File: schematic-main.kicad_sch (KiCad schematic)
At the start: 14 parts, among them J1 Fell_Cell_Conn_01x02_Pin, J2 CAN, J3 P_Valve, J4 Fan_2, J5 PWM_Out, J6 Fan_1, J7 Axilary_Out, J8 Temp, J9 Analog_In, P1 USB_C_Plug_USB2.0

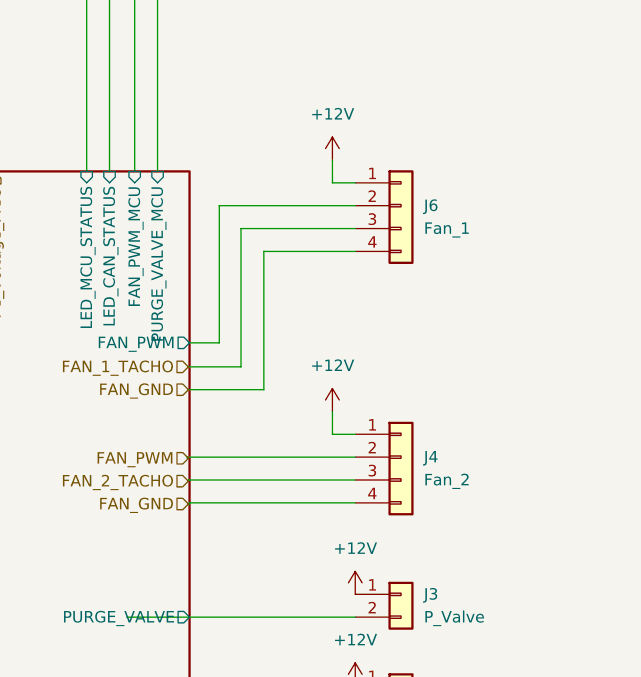
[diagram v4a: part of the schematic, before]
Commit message: First pcb, change fan conector
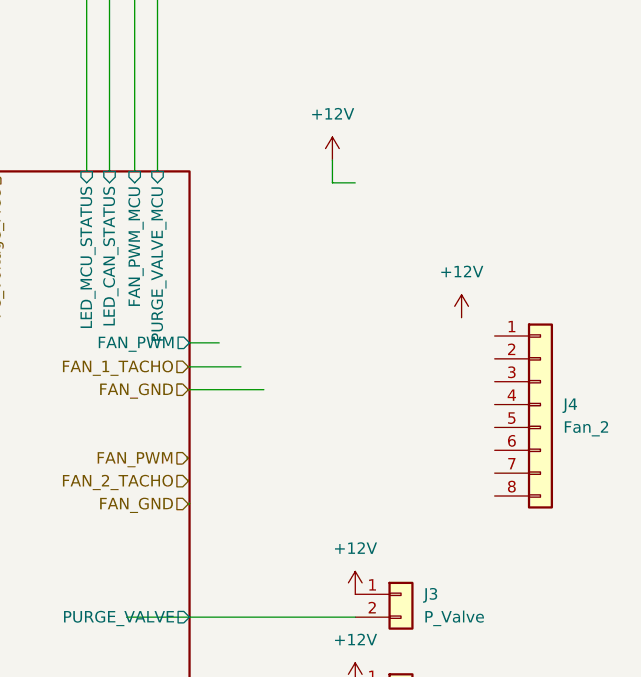
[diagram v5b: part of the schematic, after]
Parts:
- removed J6: Fan_1, symbol Connector_Generic:Conn_01x04
- J1, J2, J3, J5, J7, J8, J9: footprint (none) -> Connector_Molex:Molex_Mini-Fit_Jr_5569-02A2_2x01_P4.20mm_Horizontal
- J4: footprint (none) -> Connector_Molex:Molex_Mini-Fit_Jr_5569-04A1_4x02_P4.20mm_Horizontal; symbol Connector_Generic:Conn_01x04 -> Connector_Generic:Conn_01x08
- P1: footprint (none) -> Connector_USB:2169900002
- R1, R2, R3, R4: footprint (none) -> Resistor_SMD:R_1206_3216Metric
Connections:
- net +12V: no longer J4.1 (Pin_1)
- net FAN_2_TACHO: no longer J4.3 (Pin_3)
- net FAN_GND: no longer J4.4 (Pin_4)
- net FAN_PWM: no longer J4.2 (Pin_2)
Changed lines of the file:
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@@
-    (stroke (width 0) (type default))
-  )
-  (wire (pts (xy 191.77 125.857) (xy 191.77 110.49))
     (stroke (width 0) (type default))
   )
@@
     (stroke (width 0) (type default))
   )
-  (wire (pts (xy 194.31 113.03) (xy 204.47 113.03))
-    (stroke (width 0) (type default))
-  )
-  (wire (pts (xy 204.47 133.35) (xy 201.93 133.35))
-    (stroke (width 0) (type default))
-  )
-  (wire (pts (xy 201.93 133.35) (xy 201.93 130.81))
-    (stroke (width 0) (type default))
-  )
-  (wire (pts (xy 189.357 107.95) (xy 204.47 107.95))
-    (stroke (width 0) (type default))
-  )
   (wire (pts (xy 73.66 107.95) (xy 134.62 107.95))
     (stroke (width 0) (type default))
@@
     (stroke (width 0) (type default))
   )
-  (wire (pts (xy 185.801 135.89) (xy 204.47 135.89))
-    (stroke (width 0) (type default))
-  )
   (wire (pts (xy 147.32 81.28) (xy 147.32 104.14))
     (stroke (width 0) (type default))
@@
     (stroke (width 0) (type default))
   )
-  (wire (pts (xy 185.928 138.43) (xy 204.47 138.43))
-    (stroke (width 0) (type default))
-  )
-  (wire (pts (xy 194.31 128.397) (xy 194.31 113.03))
-    (stroke (width 0) (type default))
-  )
   (wire (pts (xy 134.62 152.4) (xy 129.54 152.4))
     (stroke (width 0) (type default))
   )
-  (wire (pts (xy 186.055 140.97) (xy 204.47 140.97))
-    (stroke (width 0) (type default))
-  )
   (wire (pts (xy 121.539 135.89) (xy 134.493 135.89))
     (stroke (width 0) (type default))
   )
-  (wire (pts (xy 191.77 110.49) (xy 204.47 110.49))
-    (stroke (width 0) (type default))
-  )
-  (wire (pts (xy 185.801 136.017) (xy 185.801 135.89))
+  (wire (pts (xy 185.801 135.89) (xy 185.801 136.017))
     (stroke (width 0) (type default))
   )
@@
     (stroke (width 0) (type default))
   )
-  (wire (pts (xy 185.928 138.557) (xy 185.928 138.43))
+  (wire (pts (xy 185.928 138.43) (xy 185.928 138.557))
     (stroke (width 0) (type default))
   )
@@
     (stroke (width 0) (type default))
   )
-  (wire (pts (xy 186.055 141.097) (xy 186.055 140.97))
-    (stroke (width 0) (type default))
-  )
-  (wire (pts (xy 189.357 107.95) (xy 189.357 123.19))
+  (wire (pts (xy 186.055 140.97) (xy 186.055 141.097))
     (stroke (width 0) (type default))
   )
@@
     )
   )
-  (symbol (lib_id "power:+12V") (at 201.93 130.81 0) (unit 1)
+  (symbol (lib_id "power:+12V") (at 216.281 120.396 0) (unit 1)
     (in_bom yes) (on_board yes) (dnp no)
-    (property "Reference" "#PWR055" (at 201.93 134.62 0)
-      (effects (font (size 1.27 1.27)) hide)
-    )
-    (property "Value" "+12V" (at 201.93 125.73 0)
-      (effects (font (size 1.27 1.27)))
-    )
-    (property "Footprint" "" (at 201.93 130.81 0)
-      (effects (font (size 1.27 1.27)) hide)
-    )
-    (property "Datasheet" "" (at 201.93 130.81 0)
+    (property "Reference" "#PWR055" (at 216.281 124.206 0)
+      (effects (font (size 1.27 1.27)) hide)
+    )
+    (property "Value" "+12V" (at 216.281 115.316 0)
+      (effects (font (size 1.27 1.27)))
+    )
+    (property "Footprint" "" (at 216.281 120.396 0)
+      (effects (font (size 1.27 1.27)) hide)
+    )
+    (property "Datasheet" "" (at 216.281 120.396 0)
       (effects (font (size 1.27 1.27)) hide)
     )
@@
       (effects (font (size 1.27 1.27)) (justify left))
     )
-    (property "Footprint" "" (at 117.094 146.304 0)
+    (property "Footprint" "Connector_Molex:Molex_Mini-Fit_Jr_5569-02A2_2x01_P4.20mm_Horizontal" (at 117.094 146.304 0)
       (effects (font (size 1.27 1.27)) hide)
     )
@@
       (effects (font (size 1.27 1.27)))
     )
-    (property "Footprint" "" (at 97.79 60.96 0)
+    (property "Footprint" "Connector_USB:2169900002" (at 97.79 60.96 0)
       (effects (font (size 1.27 1.27)) hide)
     )
@@
     )
   )
-  (symbol (lib_id "Connector_Generic:Conn_01x04") (at 209.55 107.95 0) (unit 1)
-    (in_bom yes) (on_board yes) (dnp no) (fields_autoplaced)
-    (property "Reference" "J6" (at 212.09 107.95 0)
-      (effects (font (size 1.27 1.27)) (justify left))
-    )
-    (property "Value" "Fan_1" (at 212.09 110.49 0)
-      (effects (font (size 1.27 1.27)) (justify left))
-    )
-    (property "Footprint" "" (at 209.55 107.95 0)
-      (effects (font (size 1.27 1.27)) hide)
-    )
-    (property "Datasheet" "~" (at 209.55 107.95 0)
-      (effects (font (size 1.27 1.27)) hide)
-    )
-    (pin "1")
-    (pin "2")
-    (pin "3")
-    (pin "4")
-    (instances
-      (project "schematic-main"
-        (path "/c9ad7189-d3b2-414a-9743-efd8e57cd755"
-          (reference "J6") (unit 1)
-        )
-      )
-    )
-  )
   (symbol (lib_id "Device:R") (at 116.84 54.61 90) (unit 1)
     (in_bom yes) (on_board yes) (dnp no)
@@
       (effects (font (size 1.27 1.27)))
     )
-    (property "Footprint" "" (at 116.84 56.388 90)
+    (property "Footprint" "Resistor_SMD:R_1206_3216Metric" (at 116.84 56.388 90)
       (effects (font (size 1.27 1.27)) hide)
     )
@@
       (effects (font (size 1.27 1.27)) (justify left))
     )
-    (property "Footprint" "" (at 121.412 119.634 0)
+    (property "Footprint" "Connector_Molex:Molex_Mini-Fit_Jr_5569-02A2_2x01_P4.20mm_Horizontal" (at 121.412 119.634 0)
       (effects (font (size 1.27 1.27)) hide)
     )
@@
       (effects (font (size 1.27 1.27)) (justify left))
     )
-    (property "Footprint" "" (at 157.48 176.53 0)
+    (property "Footprint" "Connector_Molex:Molex_Mini-Fit_Jr_5569-02A2_2x01_P4.20mm_Horizontal" (at 157.48 176.53 0)
       (effects (font (size 1.27 1.27)) hide)
     )
@@
       (effects (font (size 1.27 1.27)))
     )
-    (property "Footprint" "" (at 24.13 31.75 0)
+    (property "Footprint" "Connector_Molex:Molex_Mini-Fit_Jr_5569-02A2_2x01_P4.20mm_Horizontal" (at 24.13 31.75 0)
       (effects (font (size 1.27 1.27)) hide)
     )
@@
       (effects (font (size 1.27 1.27)))
     )
-    (property "Footprint" "" (at 116.84 53.848 90)
+    (property "Footprint" "Resistor_SMD:R_1206_3216Metric" (at 116.84 53.848 90)
       (effects (font (size 1.27 1.27)) hide)
     )
@@
       (effects (font (size 1.27 1.27)) (justify left))
     )
-    (property "Footprint" "" (at 116.459 133.35 0)
+    (property "Footprint" "Connector_Molex:Molex_Mini-Fit_Jr_5569-02A2_2x01_P4.20mm_Horizontal" (at 116.459 133.35 0)
       (effects (font (size 1.27 1.27)) hide)
     )
@@
       (effects (font (size 1.27 1.27)) (justify left))
     )
-    (property "Footprint" "" (at 109.982 80.01 90)
+    (property "Footprint" "Resistor_SMD:R_1206_3216Metric" (at 109.982 80.01 90)
       (effects (font (size 1.27 1.27)) hide)
     )
@@
     )
   )
-  (symbol (lib_id "Connector_Generic:Conn_01x04") (at 209.55 135.89 0) (unit 1)
-    (in_bom yes) (on_board yes) (dnp no) (fields_autoplaced)
-    (property "Reference" "J4" (at 212.09 135.89 0)
-      (effects (font (size 1.27 1.27)) (justify left))
-    )
-    (property "Value" "Fan_2" (at 212.09 138.43 0)
-      (effects (font (size 1.27 1.27)) (justify left))
-    )
-    (property "Footprint" "" (at 209.55 135.89 0)
-      (effects (font (size 1.27 1.27)) hide)
-    )
-    (property "Datasheet" "~" (at 209.55 135.89 0)
+  (symbol (lib_id "Connector_Generic:Conn_01x08") (at 225.044 130.048 0) (unit 1)
+    (in_bom yes) (on_board yes) (dnp no) (fields_autoplaced)
+    (property "Reference" "J4" (at 227.584 130.048 0)
+      (effects (font (size 1.27 1.27)) (justify left))
+    )
+    (property "Value" "Fan_2" (at 227.584 132.588 0)
+      (effects (font (size 1.27 1.27)) (justify left))
+    )
+    (property "Footprint" "Connector_Molex:Molex_Mini-Fit_Jr_5569-04A1_4x02_P4.20mm_Horizontal" (at 225.044 130.048 0)
+      (effects (font (size 1.27 1.27)) hide)
+    )
+    (property "Datasheet" "~" (at 225.044 130.048 0)
       (effects (font (size 1.27 1.27)) hide)
     )
@@
     (pin "3")
     (pin "4")
+    (pin "5")
+    (pin "6")
+    (pin "7")
+    (pin "8")
     (instances
       (project "schematic-main"
@@
       (effects (font (size 1.27 1.27)) (justify left))
     )
-    (property "Footprint" "" (at 209.55 151.13 0)
+    (property "Footprint" "Connector_Molex:Molex_Mini-Fit_Jr_5569-02A2_2x01_P4.20mm_Horizontal" (at 209.55 151.13 0)
       (effects (font (size 1.27 1.27)) hide)
     )
@@
       (effects (font (size 1.27 1.27)) (justify left))
     )
-    (property "Footprint" "" (at 116.332 80.01 90)
+    (property "Footprint" "Resistor_SMD:R_1206_3216Metric" (at 116.332 80.01 90)
       (effects (font (size 1.27 1.27)) hide)
     )
@@
       (effects (font (size 1.27 1.27)) (justify left))
     )
-    (property "Footprint" "" (at 209.55 161.29 0)
-      (effects (font (size 1.27 1.27)) hide)
-    )
+    (property "Footprint" "Connector_Molex:Molex_Mini-Fit_Jr_5569-02A2_2x01_P4.20mm_Horizontal" (at 209.55 161.29 0)
+      (effects (font (size 1.27 1.27)) hide)
+    )

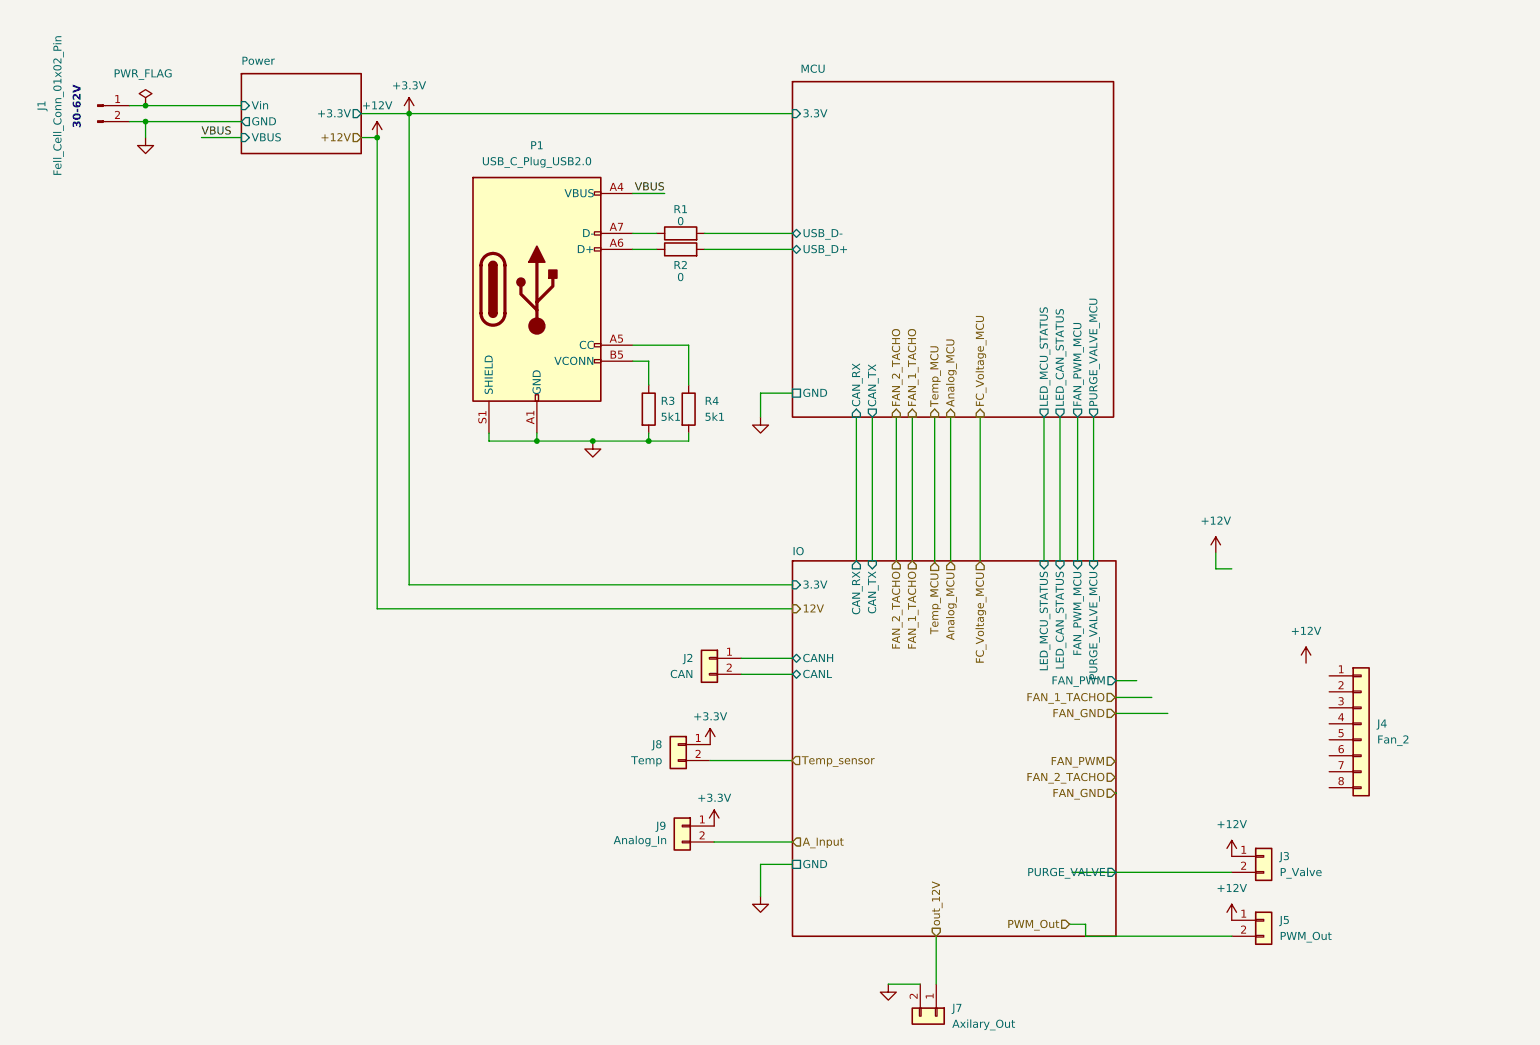
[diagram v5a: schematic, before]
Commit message: Change FC connector to 10pin & ideal diode sircuit
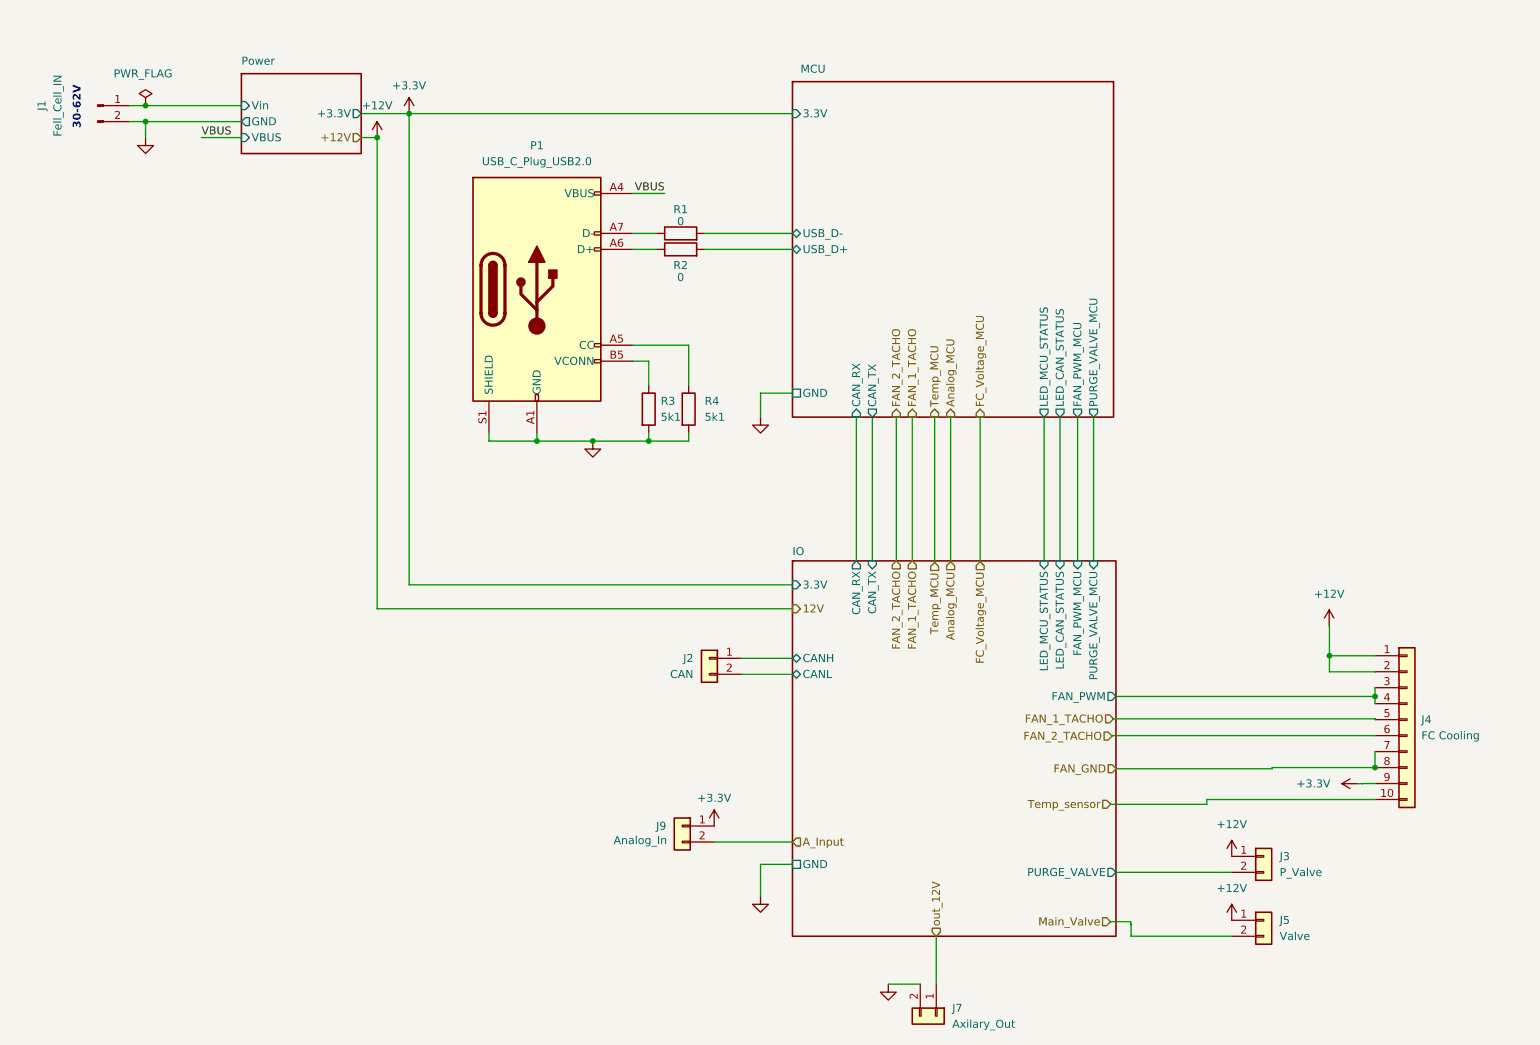
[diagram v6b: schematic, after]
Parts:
- removed J8: Temp, Connector_Molex:Molex_Mini-Fit_Jr_5569-02A2_2x01_P4.20mm_Horizontal, symbol Connector_Generic:Conn_01x02
- J1: value Fell_Cell_Conn_01x02_Pin -> Fell_Cell_IN
- J4: value Fan_2 -> FC Cooling; footprint Connector_Molex:Molex_Mini-Fit_Jr_5569-04A1_4x02_P4.20mm_Horizontal -> Connector_Molex:Molex_Mini-Fit_Jr_5569-10A1_2x05_P4.20mm_Horizontal; symbol Connector_Generic:Conn_01x08 -> Connector_Generic:Conn_01x10
- J5: value PWM_Out -> Valve
- P1: footprint Connector_USB:2169900002 -> library:2169900002
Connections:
- net +12V: now also J4.1 (Pin_1), J4.2 (Pin_2)
- net +3.3V: now also J4.9 (Pin_9)
- net FAN_1_TACHO: now also J4.5 (Pin_5)
- net FAN_2_TACHO: now also J4.6 (Pin_6)
- net FAN_GND: now also J4.7 (Pin_7), J4.8 (Pin_8)
- net IO/FAN_PWM: now also J4.3 (Pin_3), J4.4 (Pin_4)
- net IO/PURGE_VALVE: now also J3.2 (Pin_2)
- net Temp_sensor: now also J4.10 (Pin_10)
- net PWM_Out renamed Main_Valve

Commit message: Complate frist version
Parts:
- J4: symbol Connector_Generic:Conn_01x10 -> Connector_Generic:Conn_02x05_Top_Bottom
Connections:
- net FAN_2_TACHO is gone; now on net +12V: J4.6 (Pin_6)
- net Temp_sensor is gone; now on net +3.3V: J4.10 (Pin_10)
- net +12V: no longer J4.2 (Pin_2)
- net +3.3V: no longer J4.9 (Pin_9)
- net IO/FAN_PWM: now also J4.2 (Pin_2), J4.7 (Pin_7); no longer J4.3 (Pin_3), J4.4 (Pin_4)
- net A_Input renamed IO/A_Input
- net FAN_1_TACHO renamed IO/Temp_sensor
- net FAN_GND renamed IO/FAN_2_TACHO
- net IO/FAN_2_TACHO: no longer J4.7 (Pin_7)
- net Main_Valve renamed IO/Main_Valve
- net out_12V renamed IO/out_12V
- new net IO/FAN_1_TACHO: J4.3 (Pin_3)
- new net IO/FAN_GND: J4.4 (Pin_4), J4.9 (Pin_9)
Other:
- sheet IO ports: added 12V, A_Input, Analog_MCU, FAN_1_TACHO, FAN_1_TACHO_MCU, FAN_2_TACHO, FAN_2_TACHO_MCU, FAN_GND, FAN_ON_MCU, FC_Voltage_MCU, Main_Valve, Main_Valve_MCU, SC_V, Temp_MCU, Temp_sensor, out_12V; removed none
- sheet MCU ports: added Analog_MCU, FAN_1_TACHO_MCU, FAN_2_TACHO_MCU, FAN_ON_MCU, FC_Voltage_MCU, Main_Valve_MCU, Temp_MCU; removed none
- sheet Power  ports: added SC_V; removed none
- moved on the sheet: J4

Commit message: porawa library
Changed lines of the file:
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@@
     (stroke (width 0) (type default))
   )
-  (wire (pts (xy 227.3046 125.7508) (xy 227.3046 125.7))
+  (wire (pts (xy 227.3046 125.7508) (xy 227.3046 125.73))
     (stroke (width 0) (type default))
   )
@@
     (stroke (width 0) (type default))
   )
-  (wire (pts (xy 227.3046 125.7) (xy 186.055 125.7))
+  (wire (pts (xy 227.3046 125.73) (xy 186.055 125.73))
     (stroke (width 0) (type default))
   )
@@
       (effects (font (size 1.27 1.27)) (justify left))
     )
-    (pin "FAN_PWM" output (at 186.055 125.7 0)
+    (pin "FAN_PWM" output (at 186.055 125.73 0)
       (effects (font (size 1.27 1.27)) (justify right))
     )
